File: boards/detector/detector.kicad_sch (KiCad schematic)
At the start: 2 parts, among them J1 Conn_01x04, U1 ESP32-DevKitC

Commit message: testing detector schematic and pcb
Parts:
- added J1: ST7920, Connector_PinSocket_2.54mm:PinSocket_1x20_P2.54mm_Vertical, symbol Connector_Generic:Conn_01x20
- added R1, R2: 1K, Resistor_SMD:R_0603_1608Metric, symbol Device:R
- added SW1: Button, Button_Switch_THT:SW_SPST_Omron_B3F-40xx, symbol Switch:SW_Push
- S1: renamed from J1; value Conn_01x04 -> SCD41; footprint Connector_PinHeader_1.00mm:PinHeader_1x04_P1.00mm_Vertical -> Connector_PinSocket_2.54mm:PinSocket_1x04_P2.54mm_Vertical
- U1: value ESP32-DevKitC -> ESP32
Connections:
- net I2C SDA: now reaches S1.1 (SDA)
- net I2C SDA: now also U1.33 (GPIO21)
- net I2C SCL: now reaches S1.2 (SCL)
- net I2C SCL: now also U1.36 (GPIO22)
- net VCC: now reaches S1.3 (VCC)
- net VCC: now also U1.19 (5V), J1.2 (VCC), R2.2
- net GND: now reaches S1.4 (GND)
- net GND: now also U1.14 (GND), U1.32 (GND), U1.38 (GND), J1.1 (GND), J1.15 (PSB), J1.20 (BLK), SW1.1
- net +3V3: now reaches U1.1 (3V3)
- net BUTTON: now reaches U1.26 (ADC2_CH0/GPIO4)
- net BUTTON: now also R2.1, SW1.2
- net BACKLIGHT: now reaches U1.27 (GPIO16)
- net BACKLIGHT: now also R1.1
- net RS: now reaches U1.28 (GPIO17)
- net RS: now also J1.4 (RS)
- net E: now reaches U1.30 (GPIO18)
- net E: now also J1.6 (E)
- net R/W: now reaches U1.37 (GPIO23)
- net R/W: now also J1.5 (R/W)
- new net: J1.19 (BLA), R1.2
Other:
- note added: "Display"
- note added: "Interface"
- note added: "Power"
- note added: "Processor"
- note added: "Sensors"
- moved on the sheet: S1, U1

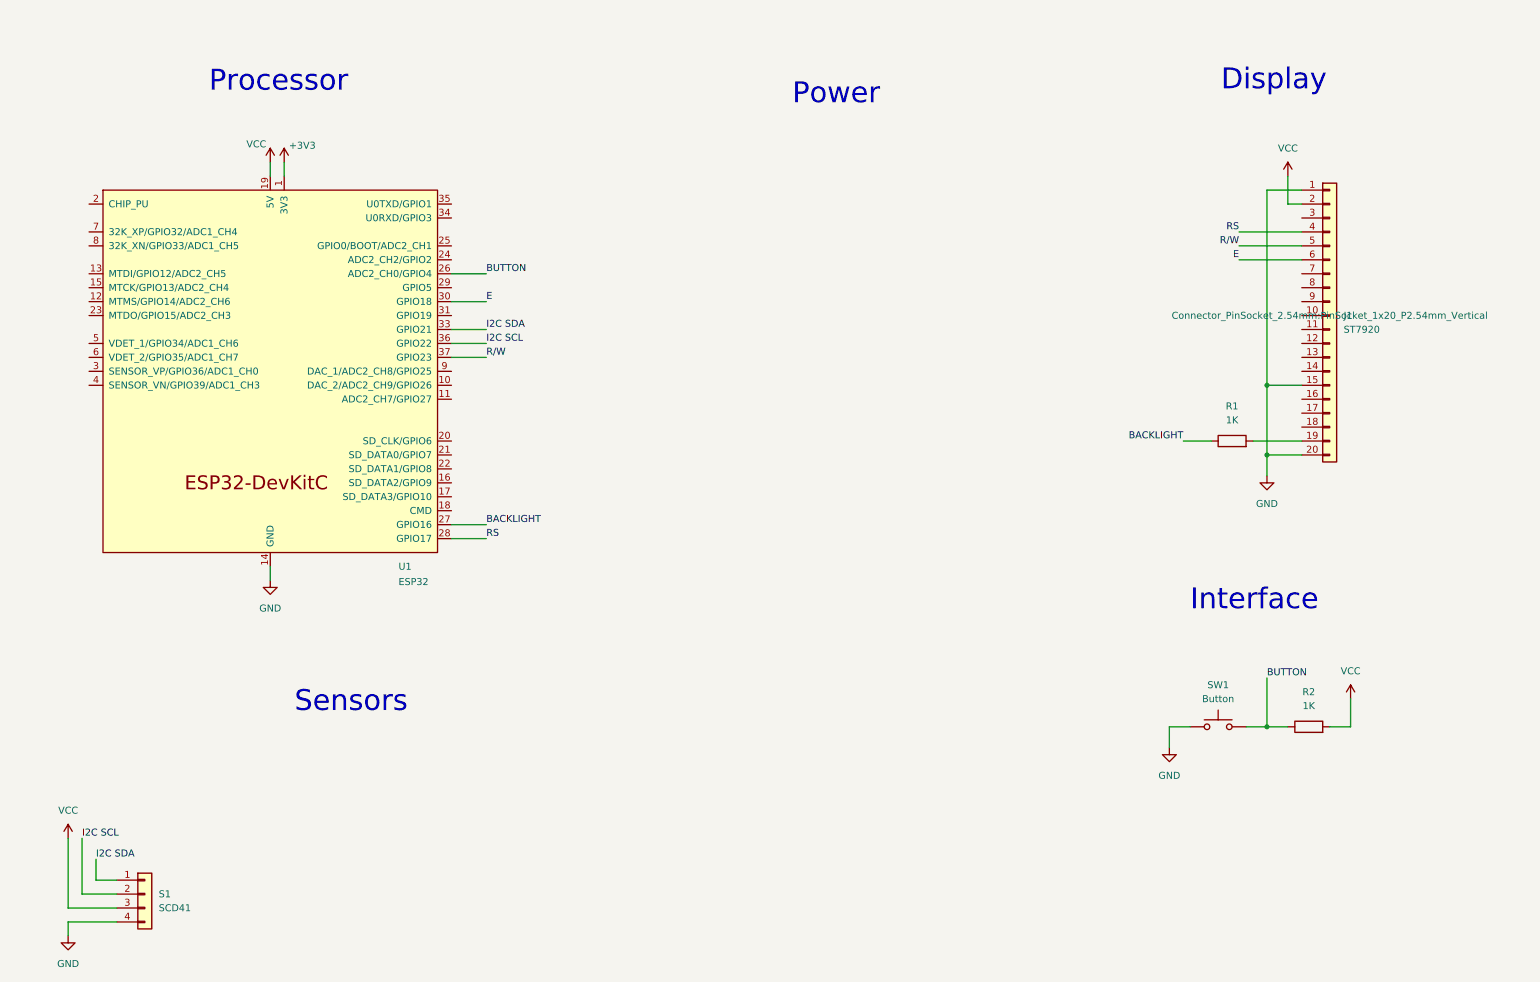
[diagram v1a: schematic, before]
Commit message: updated detector schematic
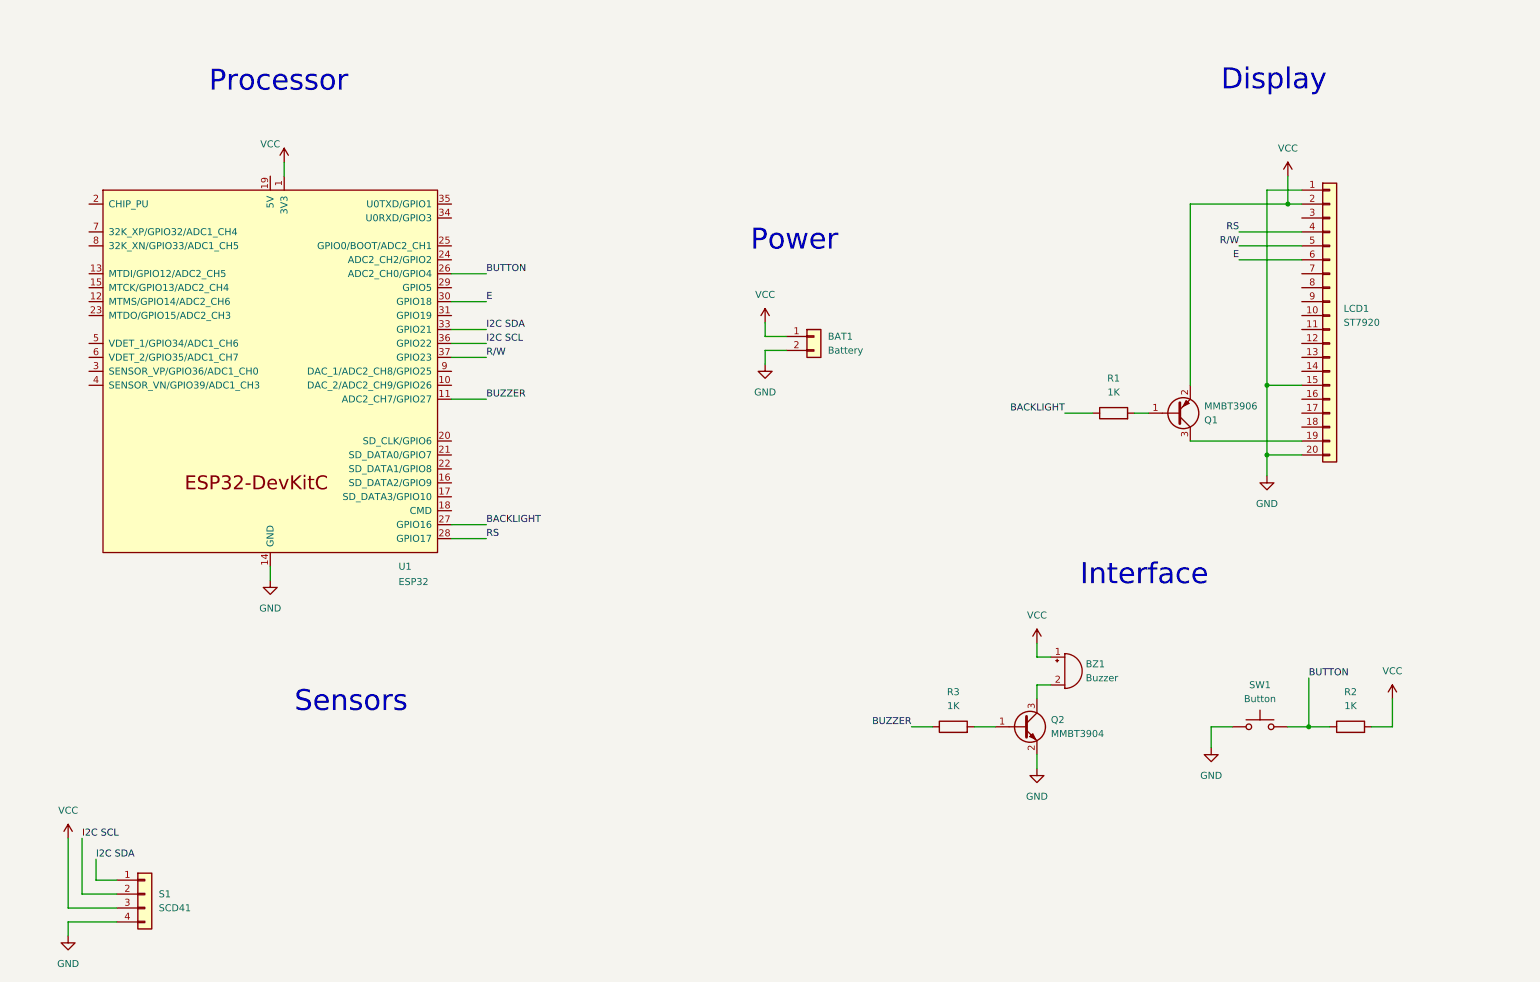
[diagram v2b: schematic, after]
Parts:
- added BAT1: Battery, Connector_JST:JST_XH_B2B-XH-A_1x02_P2.50mm_Vertical, symbol Connector_Generic:Conn_01x02
- added BZ1: Buzzer, Buzzer_Beeper:Buzzer_12x9.5RM7.6, symbol Device:Buzzer
- added Q1: MMBT3906, Package_TO_SOT_SMD:SOT-23, symbol Transistor_BJT:MMBT3906
- added Q2: MMBT3904, Package_TO_SOT_SMD:SOT-23, symbol Transistor_BJT:MMBT3904
- added R3: 1K, Resistor_SMD:R_0805_2012Metric_Pad1.20x1.40mm_HandSolder, symbol Device:R
- R1, R2: footprint Resistor_SMD:R_0603_1608Metric -> Resistor_SMD:R_0805_2012Metric_Pad1.20x1.40mm_HandSolder
- renumbered J1 to LCD1
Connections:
- net +3V3 is gone; now on net VCC: U1.1 (3V3)
- net GND: now also BAT1.2 (GND), Q2.2 (E)
- net VCC: now also BAT1.1 (VCC), BZ1.1 (+), Q1.2 (E); no longer U1.19 (5V)
- net at R1.2: now also Q1.1 (B); no longer LCD1.19 (BLA)
- net BUZZER: now reaches U1.11 (ADC2_CH7/GPIO27)
- net BUZZER: now also R3.1
- new net: LCD1.19 (BLA), Q1.3 (C)
- new net: Q2.1 (B), R3.2
- new net: BZ1.2 (-), Q2.3 (C)
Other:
- moved on the sheet: R1, R2, SW1

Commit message: compacting pcb and fixing sizes
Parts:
- LCD1: footprint Connector_PinSocket_2.54mm:PinSocket_1x20_P2.54mm_Vertical -> Library:ST7920
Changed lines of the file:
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@@
 			)
 		)
-		(property "Footprint" "Connector_PinSocket_2.54mm:PinSocket_1x20_P2.54mm_Vertical"
+		(property "Footprint" "Library:ST7920"
 			(at 262.89 74.9299 0)
 			(effects

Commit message: more work done on the detector board
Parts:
- removed BAT1: Battery, Connector_JST:JST_XH_B2B-XH-A_1x02_P2.50mm_Vertical, symbol Connector_Generic:Conn_01x02
- removed Q1: MMBT3906, Package_TO_SOT_SMD:SOT-23, symbol Transistor_BJT:MMBT3906
- removed Q2: MMBT3904, Package_TO_SOT_SMD:SOT-23, symbol Transistor_BJT:MMBT3904
- added BAT1: Battery, Connector_JST:JST_XH_S4B-XH-A_1x04_P2.50mm_Horizontal, symbol Connector_Generic:Conn_01x04
- added J1: CO, Library:DFRobot Sensor, symbol Connector_Generic:Conn_01x03
- added J2: Smoke, Library:DFRobot Sensor, symbol Connector_Generic:Conn_01x03
- added Q1, Q2: MMBT2222A, Package_TO_SOT_SMD:SOT-23, symbol Transistor_BJT:MMBT2222A
- R1, R2, R3: value 1K -> 10KΩ
- S1: footprint Connector_PinSocket_2.54mm:PinSocket_1x04_P2.54mm_Vertical -> Library:SCD41
- SW1: footprint Button_Switch_THT:SW_SPST_Omron_B3F-40xx -> Library:Button
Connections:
- net BACKLIGHT: now also R1.2; no longer R1.1
- net GND: now also S1.1 (GND), BAT1.1 (Pin_1), J1.1 (GND), J2.1 (GND), Q1.2 (E), Q2.2 (E); no longer LCD1.20 (BLK), S1.4 (GND)
- net I2C SCL: now also S1.3 (SCL); no longer S1.2 (SCL)
- net I2C SDA: now also S1.4 (SDA); no longer S1.1 (SDA)
- net VCC: now also LCD1.18 (VOUT), S1.2 (VCC), BAT1.2 (Pin_2), J1.2 (VCC), J2.2 (VCC); no longer S1.3 (VCC)
- net at LCD1.19 (BLA): now also Q1.3 (C)
- net at R3.2: now also Q2.1 (B)
- net at BZ1.2 (-): now also Q2.3 (C)
- net REF ON: now reaches U1.3 (SENSOR_VP/GPIO36/ADC1_CH0)
- net REF ON: now also BAT1.3 (Pin_3)
- net REF BAT: now reaches U1.4 (SENSOR_VN/GPIO39/ADC1_CH3)
- net REF BAT: now also BAT1.4 (Pin_4)
- net SMOKE: now reaches U1.5 (VDET_1/GPIO34/ADC1_CH6)
- net SMOKE: now also J2.3 (A)
- net CO: now reaches U1.6 (VDET_2/GPIO35/ADC1_CH7)
- net CO: now also J1.3 (A)
- new net: Q1.1 (B), R1.1
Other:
- company: (none) -> Caldas
- title: (none) -> Detector
- moved on the sheet: BZ1, LCD1, R1, R2, R3, S1, SW1

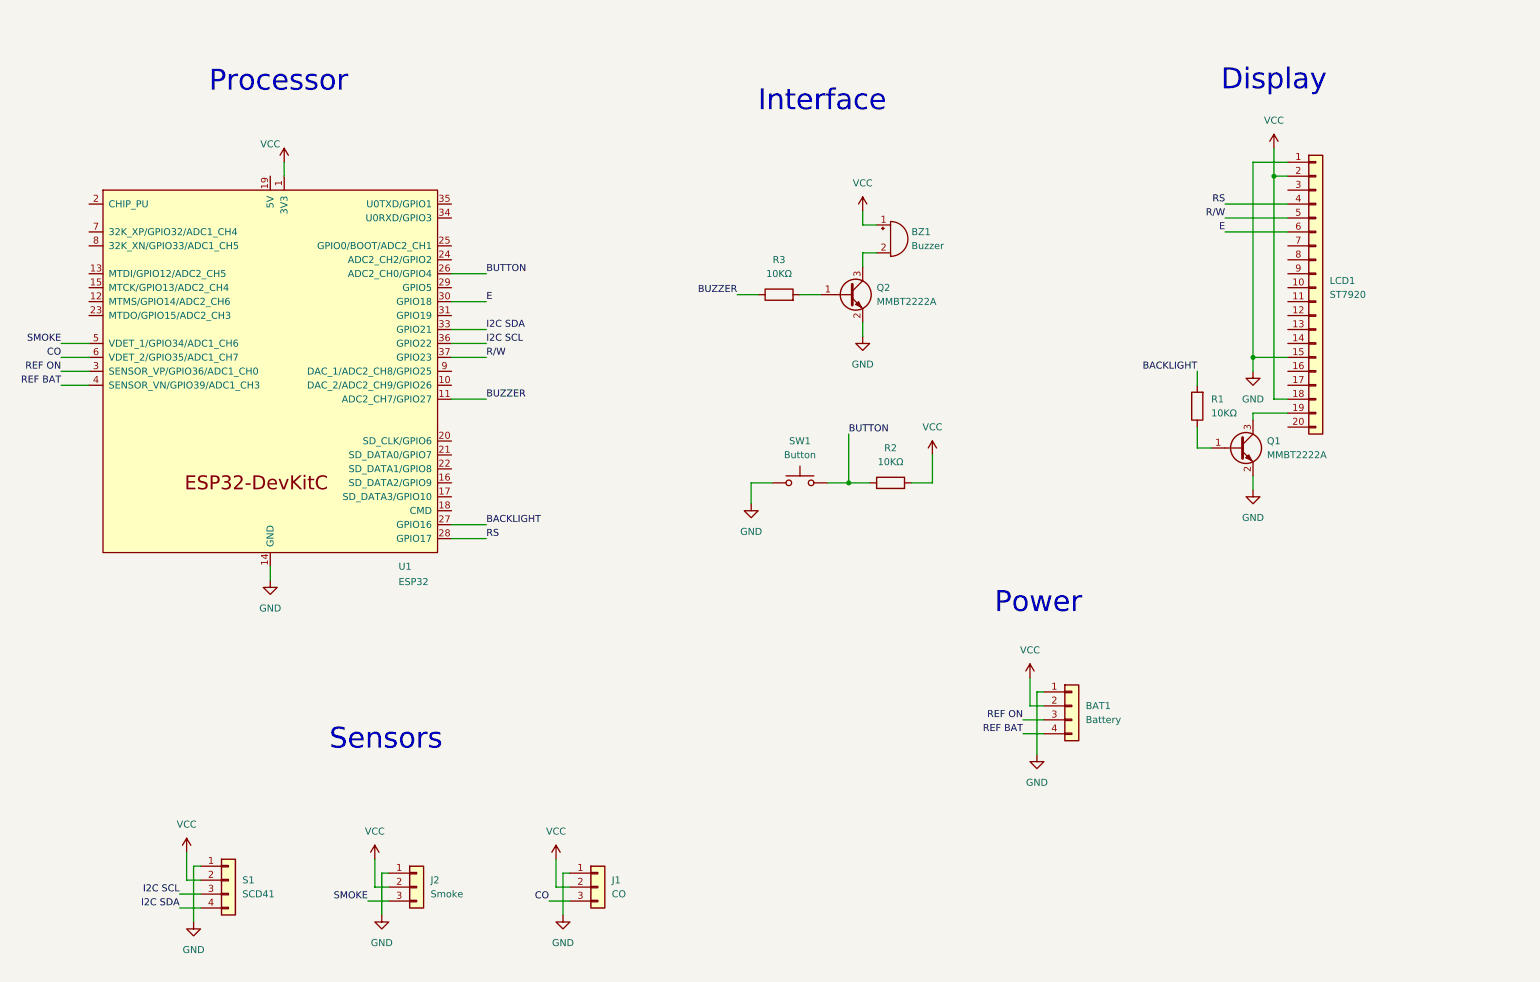
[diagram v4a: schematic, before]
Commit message: updated detector schematic
LCD pins
sensing voltage dividers
buzzer footprint
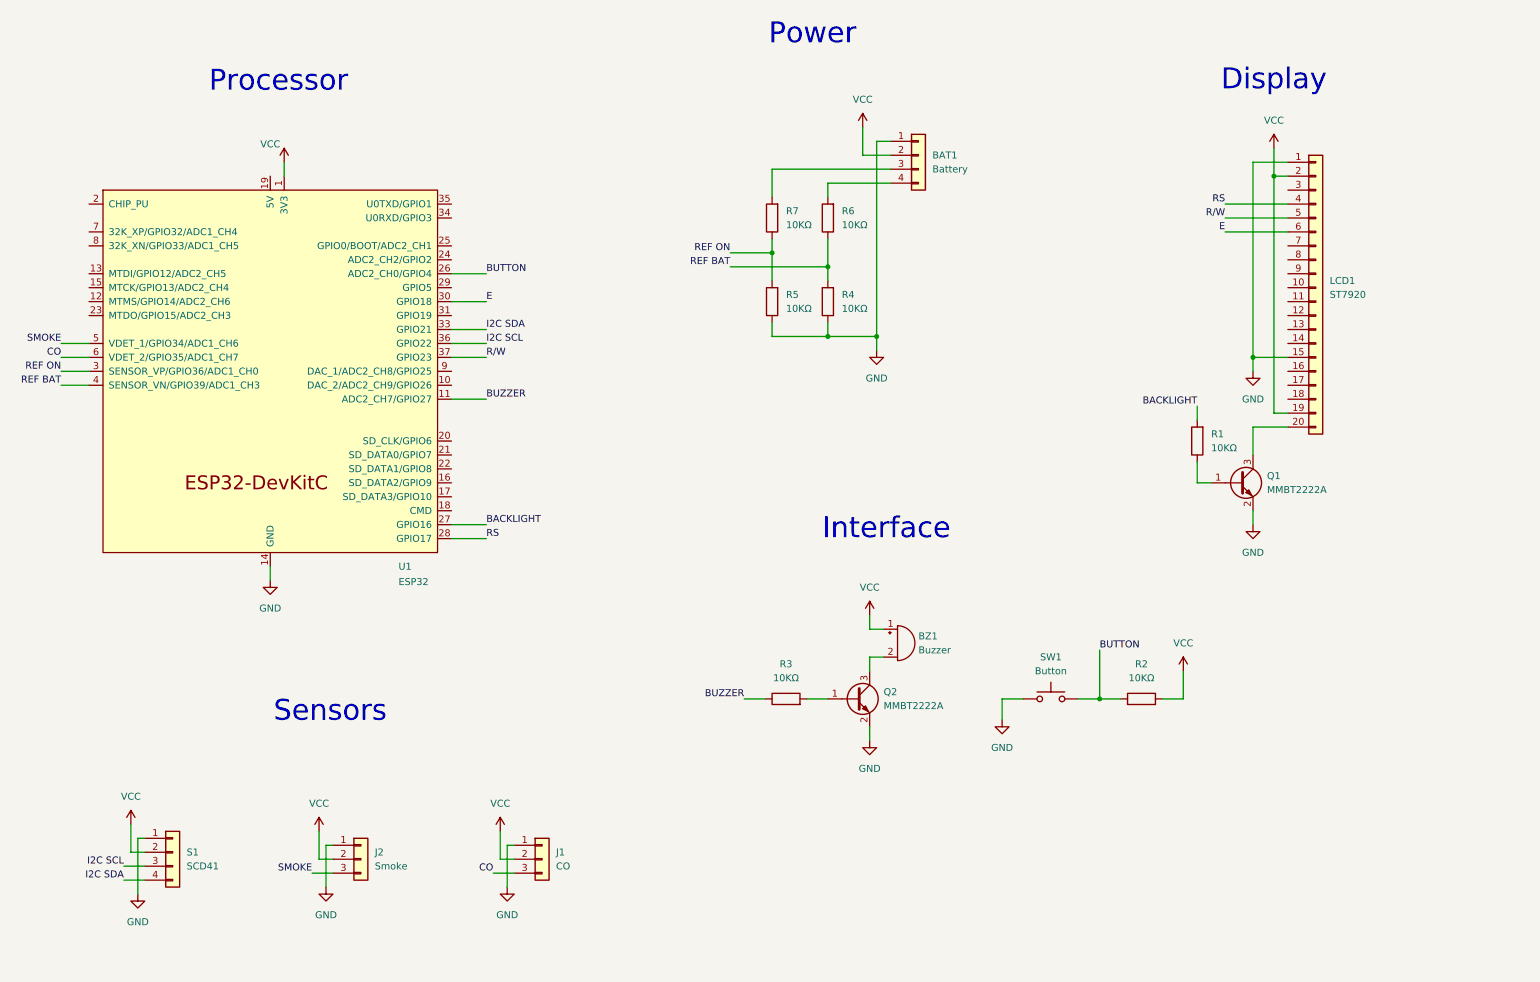
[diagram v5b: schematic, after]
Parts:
- added R4, R5, R6, R7: 10KΩ, Resistor_SMD:R_0805_2012Metric_Pad1.20x1.40mm_HandSolder, symbol Device:R
- BZ1: footprint Buzzer_Beeper:Buzzer_12x9.5RM7.6 -> Buzzer_Beeper:Buzzer_TDK_PS1240P02BT_D12.2mm_H6.5mm
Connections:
- net GND: now also R4.1, R5.1
- net REF BAT: now also R4.2, R6.1; no longer BAT1.4 (Pin_4)
- net REF ON: now also R5.2, R7.1; no longer BAT1.3 (Pin_3)
- net VCC: now also LCD1.19 (BLA); no longer LCD1.18 (VOUT)
- net at Q1.3 (C): now also LCD1.20 (BLK); no longer LCD1.19 (BLA)
- new net: BAT1.4 (Pin_4), R6.2
- new net: BAT1.3 (Pin_3), R7.2
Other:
- moved on the sheet: BAT1, BZ1, J1, J2, Q1, Q2, R1, R2, R3, S1, SW1
